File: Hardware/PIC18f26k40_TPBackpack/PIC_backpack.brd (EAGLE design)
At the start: 45 x 57.5 mm, 63 parts, among them IC1 PIC18F2480-I/ML, T1 BT138-V, T2 BT138-V, U4 W5500, X1 332-06, X4 332-12, Y2 CRYSTAL-GROUNDEDSMD-3.2X2.5

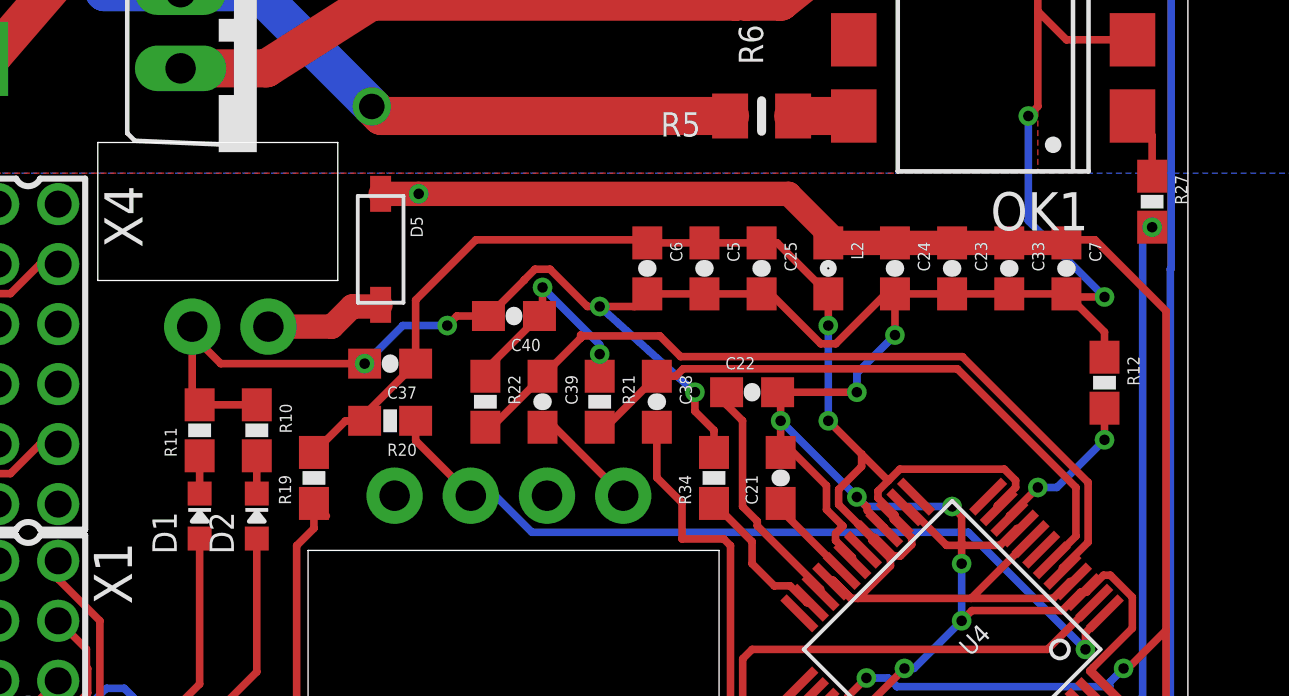
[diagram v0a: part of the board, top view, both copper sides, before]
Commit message: HEEP-299 Added silkscreen
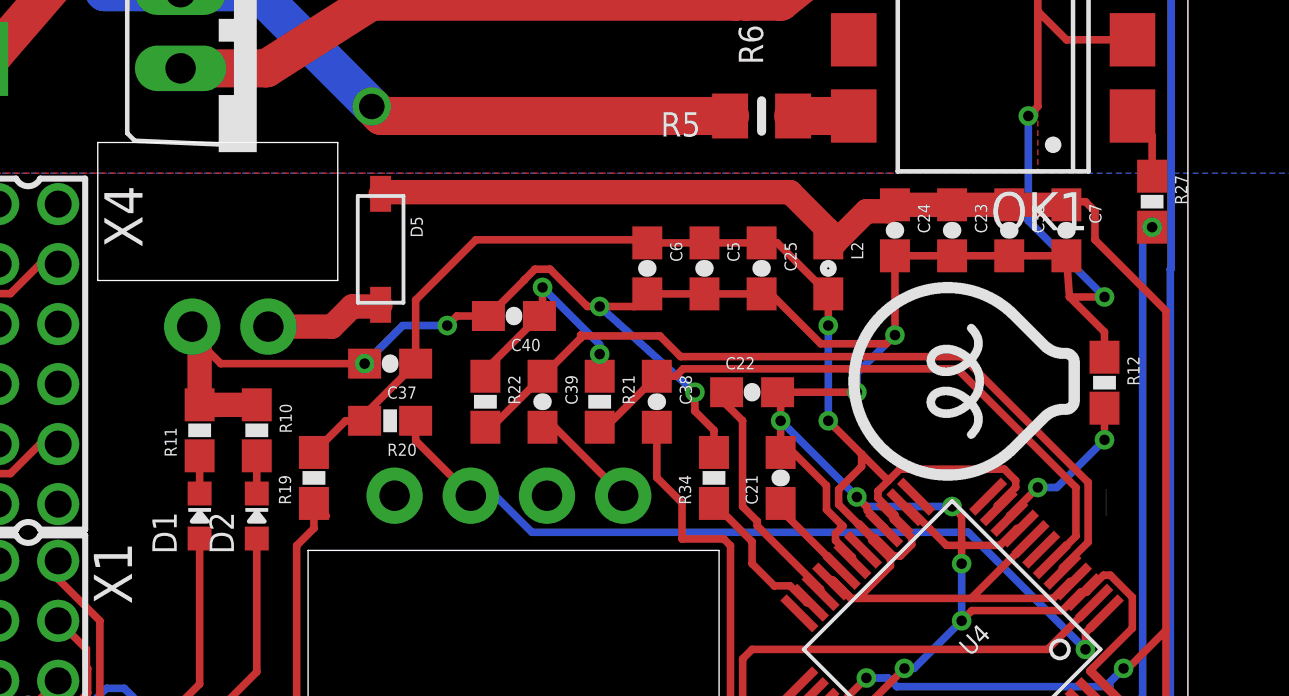
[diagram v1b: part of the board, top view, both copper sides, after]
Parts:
- added U$10: (no value), Heep:HEEPLOGOSMALL
- moved C23 1.27 mm to (37.1, 27.9)
- moved C24 1.27 mm to (35.2, 27.9)
- moved C33 1.27 mm to (39.1, 27.9)
- moved C7 1.27 mm to (41.0, 27.9)
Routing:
- net GND: track 164.8 -> 169.5 mm
- net VCC: track 123.4 -> 122.8 mm, vias 4 -> 3
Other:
- board text added: "3.3V"
- board text added: "GND"
- board text added: "GND | RB1"
- board text added: "GND | RB2"
- board text added: "GND | RB3"
- board text added: "RA1 | RA0"
- board text added: "RB5 | RB4"

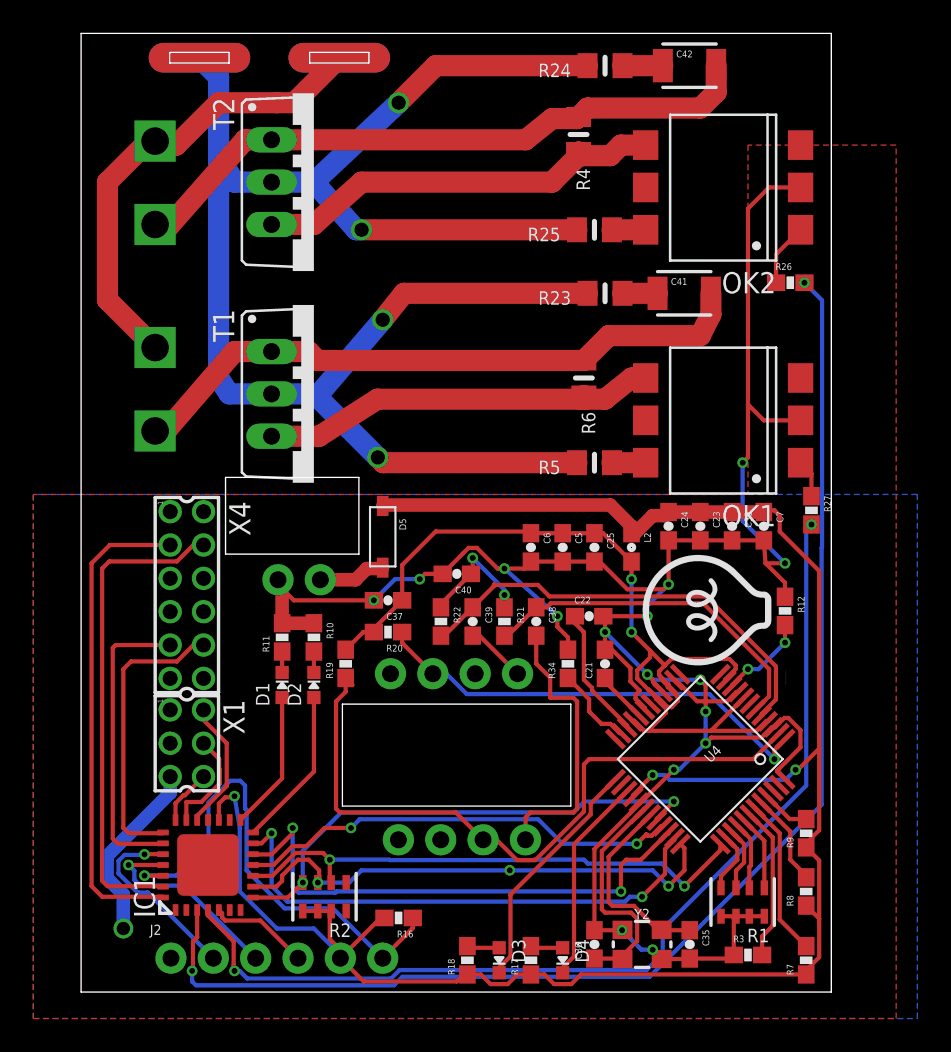
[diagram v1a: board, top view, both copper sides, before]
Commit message: Fixed DRC issues and modified seeed gerber generator to exclude tNames
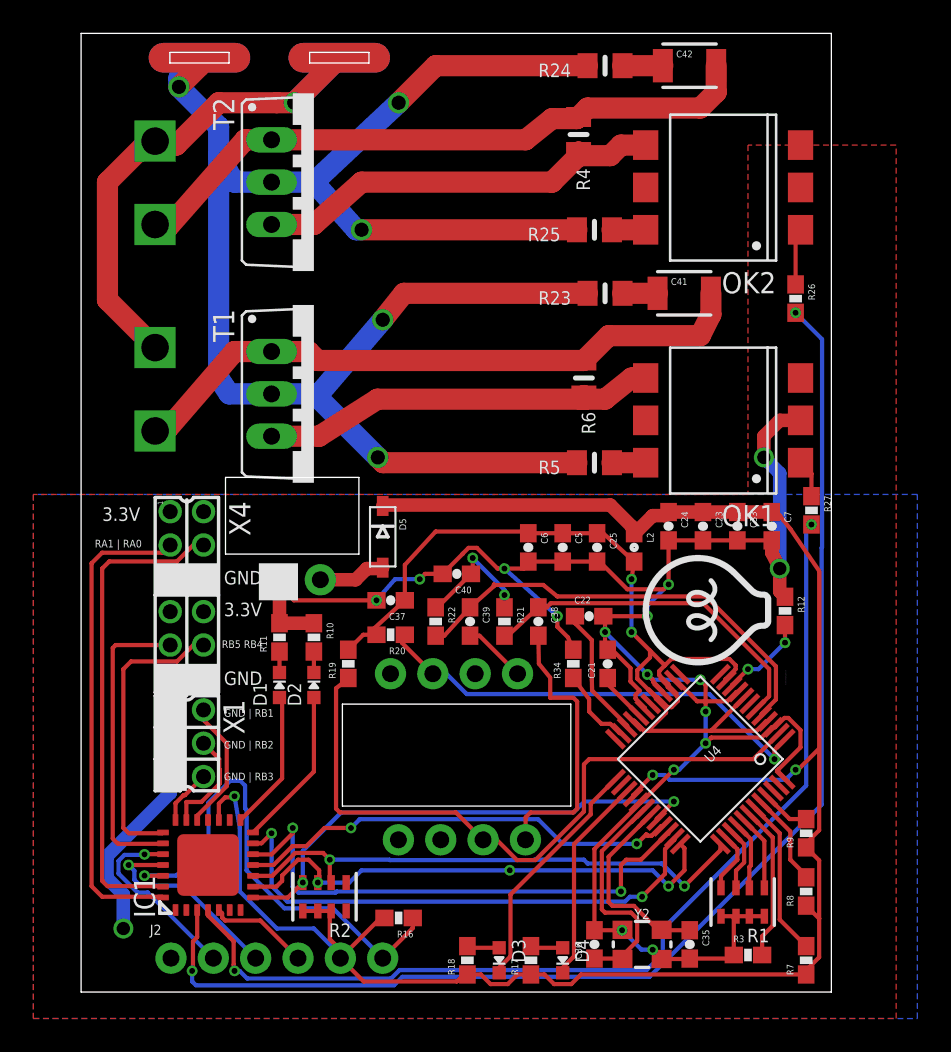
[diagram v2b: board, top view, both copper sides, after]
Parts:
- moved R26 1.00 mm to (42.9, 41.6), turned to 270 degrees
- moved C7 0.48 mm to (41.4, 27.9)
- moved R22 0.32 mm to (21.3, 22.2)
- moved R34 0.32 mm to (29.5, 19.7)
- moved C33 0.32 mm to (39.4, 27.9)
- moved R20 0.22 mm to (18.6, 21.4)
- moved C25 0.16 mm to (31.0, 26.7)
- moved C37 0.16 mm to (18.6, 23.5)
- moved C39 0.16 mm to (23.3, 22.2)
- moved C6 0.16 mm to (26.8, 26.7)
- moved R19 0.16 mm to (16.0, 19.7)
- moved D1 0.16 mm to (11.9, 18.4)
- moved R11 0.16 mm to (11.9, 21.3)
- moved C21 0.16 mm to (31.6, 19.7)
- moved C23 0.16 mm to (37.3, 27.9)
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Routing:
- net GND: track 169.5 -> 150.0 mm
- net NEUTRAL: track 28.3 -> 32.1 mm, vias 0 -> 1
- net HOT: track 105.4 -> 108.6 mm, vias 4 -> 5
- net RA4: track 78.5 -> 76.9 mm
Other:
- board text added: "RB5 RB4"
- board text removed: "RB5 | RB4"

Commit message: HEEP-410 cleaned up values, corrected AC circuit res val to 178, diode to 51ohms
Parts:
- C22: value 10nF -> 0.01uF
- C40: value 10nf -> 0.01uF
- D1: value (none) -> BLUE
- D2: value (none) -> RED
- D3: value (none) -> GREEN
- D4: value (none) -> YELLOW
- R25, R5: value 100K -> 178
- R26, R27: value 175Ω -> 51
